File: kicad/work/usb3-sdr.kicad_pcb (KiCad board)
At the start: 4 copper layers, 100 x 60 mm, 231 parts, among them J1 USB3 Micro-B, J2 SMA RF IN, J3 TC2050 JTAG, J4 SMA 10MHz REF, J5 PMOD0, J6 PMOD1, K1 HFD4/5-SR, K2 HFD4/5-SR, Q1 2N7002, Q10 AO3401A, Q11 2N7002, Q2 2N7002, T1 ADT4-6T+, U1 TPS22918DBVR, U10 W25Q128JVSIQ, U11 FT601Q-B-T, U12 LFE5U-25F-6BG256C, U13 PHA-13LN+, U14 74LVC1G17, U2 TPS62A02ADRLR, U3 TPS62A02ADRLR (forced PWM), U4 TLV75525PDBVR, U5 TPS7A2018PDBVR, U6 TPS7A2033PDBVR, U7 TPS7A2018PDBVR, U8 AD9649BCPZ-80, U9 LMK61E2-100M00SIAR, Y1 30MHz 20pF X322530MSB4SI

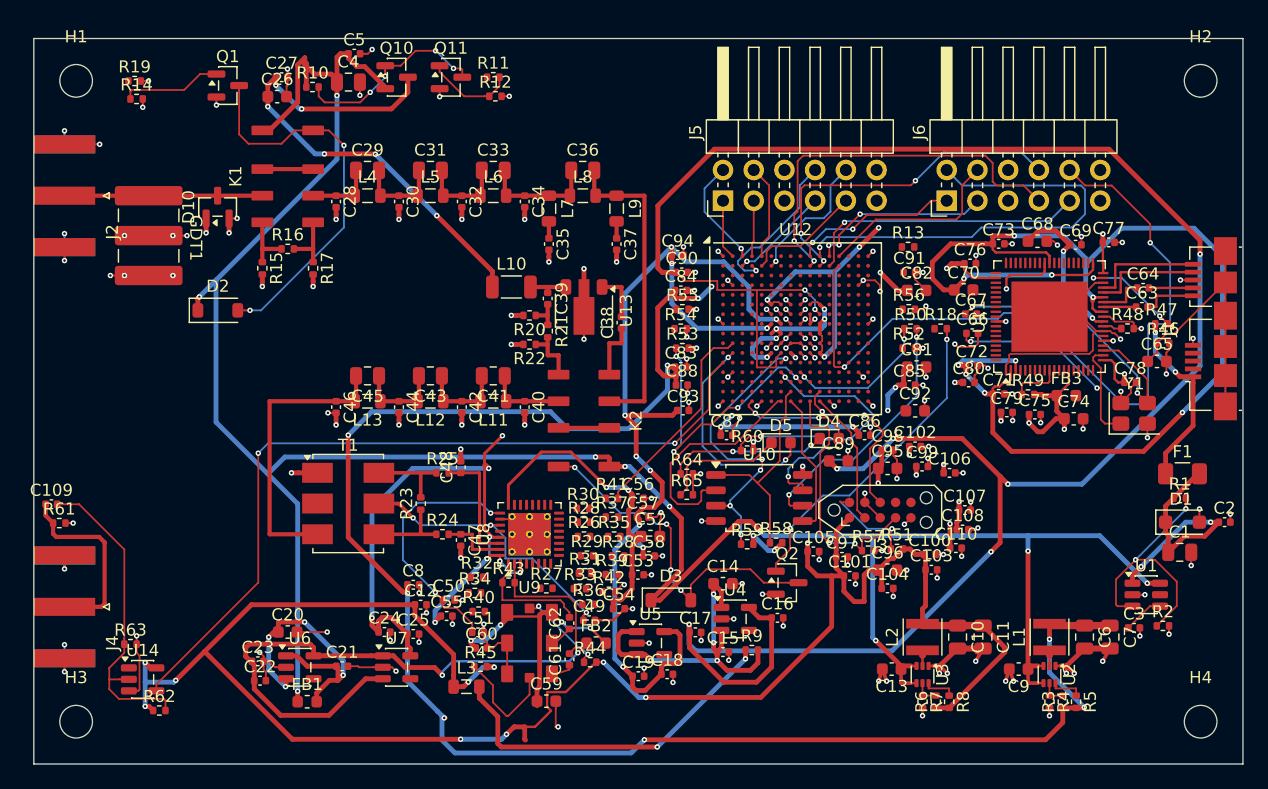
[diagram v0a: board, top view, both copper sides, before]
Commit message: Fan-out v3 applied, DeepPCB runs 3/4 adopted, bus length rules
- AGY fan-out plan v3 (with Claude's fixes) applied: power islands clear of
  the BGA escape rings, all islands fill, 0 copper conflicts.
- DeepPCB run 3 + run 4 adopted into kicad/work: 54 unconnected, DRC clean
  apart from the known SMA edge items; raw inputs/outputs in kicad/deeppcb.
- AGY ADC resistor moves applied; ADC bus re-routed, all routed FT601/ADC
  nets pass the corrected length/skew rules (notes/route).
- New tools: apply_moves.py, edge_keepout.py, lane_clear.py.

Co-Authored-By: Claude Opus 5.5 <noreply@anthropic.com>
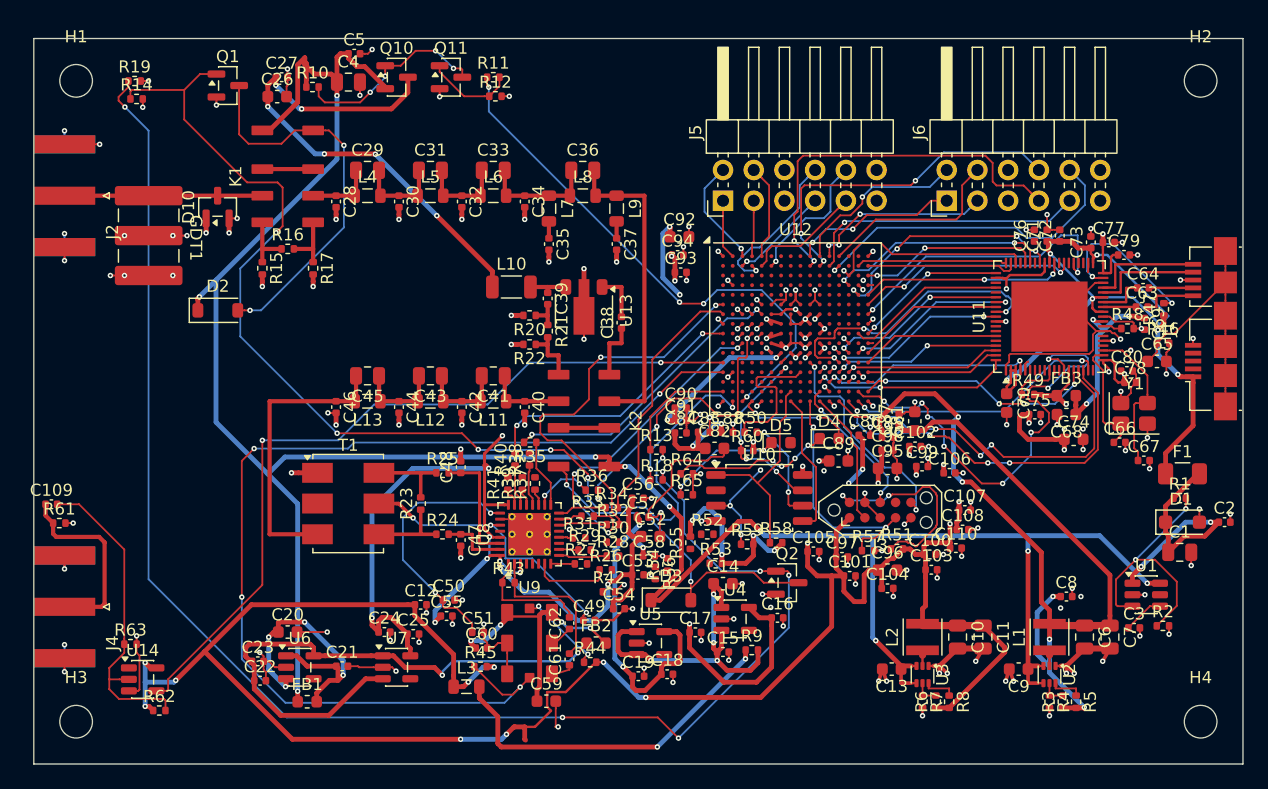
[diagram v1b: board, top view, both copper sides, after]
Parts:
- moved C8 54.0 mm to (185.4, 146.2)
- moved R56 30.2 mm to (151.4, 144.2), turned to -90 degrees
- moved R13 26.7 mm to (151.5, 134.0)
- moved R18 26.6 mm to (151.5, 136.5)
- moved C92 24.2 mm to (153.4, 116.4)
- moved R52 22.7 mm to (155.7, 141.0)
- moved C91 22.5 mm to (153.5, 131.6)
- moved C82 21.2 mm to (156.3, 133.9)
- moved R54 19.5 mm to (152.4, 143.5), turned to 90 degrees
- moved R55 19.3 mm to (154.3, 141.7), turned to 90 degrees
- moved C67 18.7 mm to (191.8, 134.9)
- moved R53 18.0 mm to (156.4, 143.4)
- moved C79 16.2 mm to (190.2, 117.9)
- moved R50 15.7 mm to (159.3, 132.6)
- moved C66 15.2 mm to (189.8, 133.4)
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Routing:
- net 2V5: track 181.4 -> 31.6 mm
- net /RF front end/Q2_G: track 27.2 -> 125.8 mm, vias 2 -> 6
- net LMK_SCL: track 9.20 -> 90.4 mm, vias 0 -> 4
- net /RF front end/Q1_G: track 8.33 -> 85.1 mm, vias 0 -> 6
- net 1V1: track 169.5 -> 99.7 mm, vias 21 -> 16
- net /USB 3 bridge/FT_1V0: track 105.0 -> 46.2 mm, vias 9 -> 4
- net 1V8_D: track 84.5 -> 38.4 mm, vias 10 -> 9
- net LNA_EN: track 0.00 -> 44.7 mm, vias 0 -> 4
- net FT_OE_N: track 0.00 -> 38.4 mm, vias 0 -> 8
- net /FPGA/PMOD1_7: track 64.9 -> 27.6 mm, vias 2 -> 1
- net ADC_D6: track 0.00 -> 32.7 mm, vias 0 -> 2
- net FT_WAKEUP_N: track 0.00 -> 31.1 mm, vias 0 -> 4
- net FT_GPIO0: track 0.00 -> 30.9 mm, vias 0 -> 4
- net ADC_D7: track 0.00 -> 27.5 mm, vias 0 -> 4
- net ADC_D10: track 0.00 -> 25.0 mm, vias 0 -> 3
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- added copper zone on In2.Cu, net 1V8_D
- added copper zone on In2.Cu, net 2V5

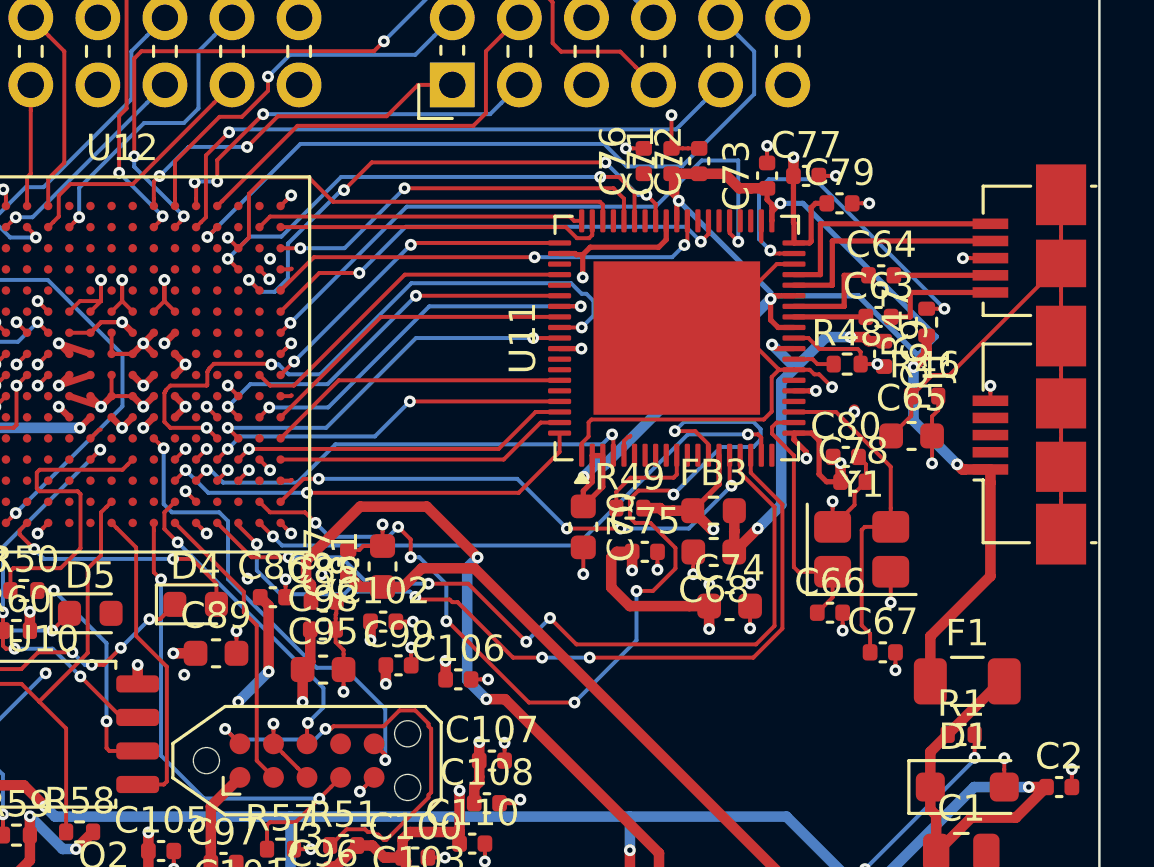
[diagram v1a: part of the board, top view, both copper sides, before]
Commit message: U11 escape plan, USB2 pair route, FT601 centre-pad vias
- AGY U11 (FT601) escape plan applied: all 19 stuck FT601 nets routed,
  every FT bus net passes length/skew (11-28 mm).
- USB2 pair hand-routed (D- crosses under D+ on B.Cu), C65 moved off the
  pair path, VBUS sense branch re-routed.
- U11 centre pad had no vias to the GND plane: 7 GND vias added.
- kicad/gen/u11_trial.py: trial any moves/rips/tracks/vias plan on a temp
  copy with real fill + DRC.
- Work board: 33 unconnected, copper DRC clean, parity 0.

Co-Authored-By: Claude Opus 5.5 <noreply@anthropic.com>
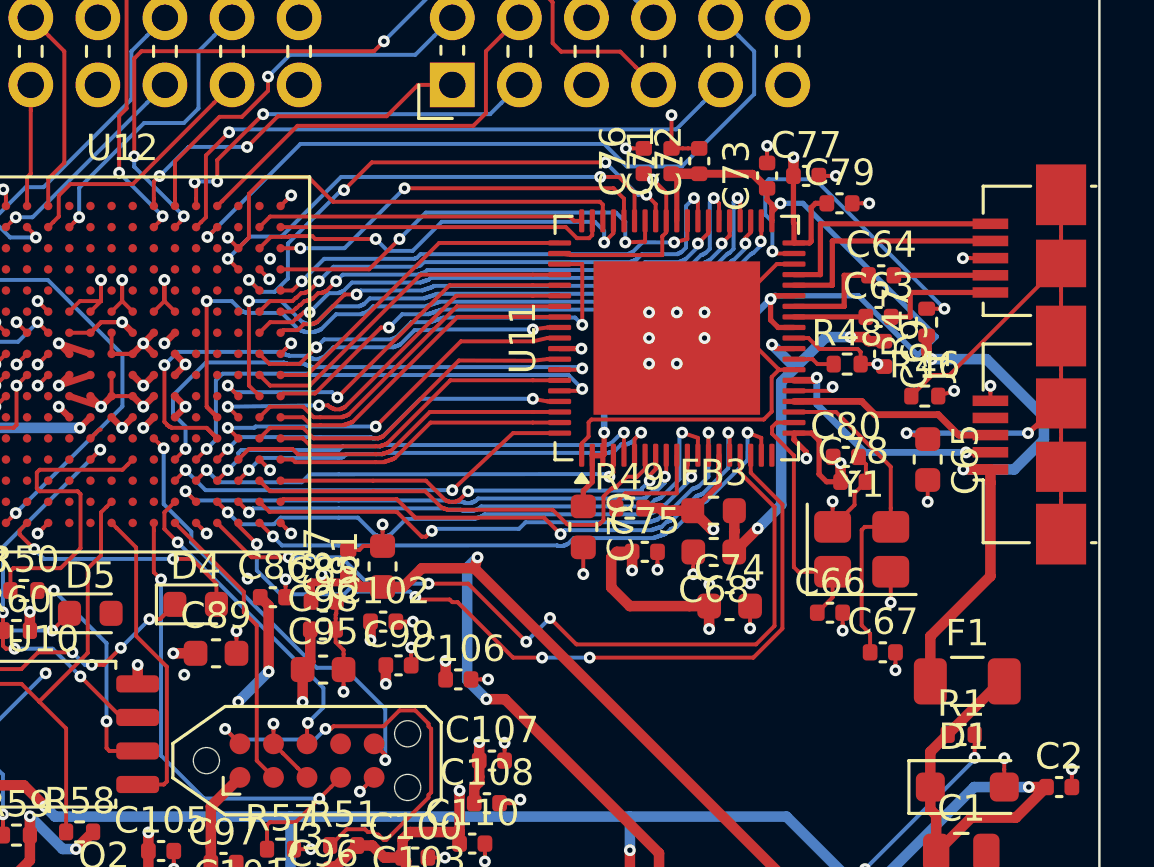
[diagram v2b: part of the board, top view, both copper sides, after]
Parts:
- moved C65 1.08 mm to (193.5, 127.6), turned to -90 degrees
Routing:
- net FT_D1: track 0.57 -> 28.5 mm, vias 1 -> 2
- net FT_D2: track 0.00 -> 26.5 mm, vias 0 -> 2
- net FT_D4: track 0.00 -> 21.3 mm, vias 0 -> 2
- net FT_D0: track 1.24 -> 22.1 mm, vias 0 -> 2
- net FT_RD_N: track 0.00 -> 20.6 mm, vias 0 -> 2
- net FT_WR_N: track 0.00 -> 20.6 mm, vias 0 -> 2
- net FT_D6: track 0.00 -> 20.1 mm, vias 0 -> 2
- net FT_RXF_N: track 0.57 -> 20.3 mm, vias 1 -> 2
- net FT_D25: track 0.57 -> 19.8 mm, vias 1 -> 2
- net FT_D27: track 0.57 -> 18.4 mm, vias 1 -> 2
- net FT_OE_N: track 38.4 -> 21.0 mm, vias 8 -> 2
- net FT_BE3: track 0.00 -> 17.2 mm
- net FT_BE2: track 0.57 -> 17.0 mm, vias 1 -> 2
- net FT_D16: track 0.00 -> 16.4 mm, vias 0 -> 2
- net FT_D9: track 0.44 -> 16.4 mm, vias 0 -> 2
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
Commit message: Route U12 south-west region: board fully routed
AGY's U12 south-west plan round 2 (ADC bus, ADC SPI, FPGA config, flash, LED1,
LMK_SDA, rail stubs) closes the last 33 connections: 0 unconnected, schematic
parity 0, no new copper DRC errors. ADC and FT601 timing pass.

- New kicad/gen/rf_spacing.py: digital copper vs RF-path copper, same layer.
  Round 1 ran ADC lines 0.21 mm beside NOTCH_OUT; round 2 keeps >= 0.65 mm
  and also clears the pre-existing REF10M / LPF2_OUT and ADC_D8 / NOTCH_OUT
  runs. Seven ADC nets run at 0.10 mm width beside NOTCH_OUT.
- In2 rect x 134-152, y 108-134 retargeted from 1V8_A to GND: it had no loads
  and its only feed was ripped by the plan (isolated copper).
- u11_trial.py also prints all still-open nets and ADC timing FAIL lines.
- DeepPCB run 5 input kept (run stopped without a revision).
- Briefs, plans and Claude's reviews in notes/u12sw/; STATUS.md updated.

Co-Authored-By: Claude Opus 5.5 <noreply@anthropic.com>
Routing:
- net ADC_SCLK: track 0.57 -> 39.9 mm, vias 1 -> 2
- net ADC_CSB: track 0.00 -> 39.0 mm, vias 0 -> 2
- net ADC_D0: track 0.57 -> 37.2 mm, vias 1 -> 2
- net ADC_SDIO: track 0.00 -> 36.1 mm, vias 0 -> 2
- net ADC_D12: track 0.57 -> 36.1 mm, vias 1 -> 2
- net LMK_SDA: track 7.10 -> 42.2 mm, vias 2 -> 7
- net ADC_D13: track 0.57 -> 33.7 mm, vias 1 -> 6
- net ADC_D2: track 0.00 -> 32.0 mm, vias 0 -> 2
- net ADC_D11: track 0.57 -> 32.2 mm, vias 1 -> 4
- net ADC_D1: track 0.57 -> 31.1 mm, vias 1 -> 2
- net ADC_D5: track 0.57 -> 30.6 mm, vias 1 -> 2
- net ADC_OR: track 0.00 -> 29.1 mm, vias 0 -> 2
- net /FPGA/FPGA_CFG0: track 0.00 -> 29.0 mm, vias 0 -> 2
- net ADC_D3: track 0.57 -> 29.2 mm, vias 1 -> 2
- net /FPGA/FPGA_DONE: track 0.00 -> 27.1 mm, vias 0 -> 2
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- removed copper zone on In2.Cu, net 1V8_A

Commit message: Remove dangling vias and stubs from the work board
8 vias connected on one layer only (1V1 x2, 2V5 x2, 3V3_D, 5V_SW, FT_D13,
LNA_EN) and 3 stubs left loose by them (3V3_D 0.1 + 1.0 mm, FT_D13 0.57 mm
escape stub). DRC after: 0 unconnected, parity 0, no dangling copper; only
the 10 SMA edge items and silk warnings remain. Timing and RF spacing
unchanged (FT_D13 16.92 mm, pass). Backup kicad/deeppcb/work_before_cleanup.

Co-Authored-By: Claude Opus 5.5 <noreply@anthropic.com>
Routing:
- net 3V3_D: track 228.3 -> 227.2 mm, vias 36 -> 35
- net FT_D13: track 17.5 -> 16.9 mm, vias 1 -> 0
- net LNA_EN: vias 3 -> 2
- net 5V_SW: vias 9 -> 8
- net 2V5: vias 7 -> 5
- net 1V1: vias 14 -> 12
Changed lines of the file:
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@@
 	)
 	(via
-		(at 184.92 147.1)
-		(size 0.45)
-		(drill 0.2)
-		(layers "F.Cu" "B.Cu")
-		(locked yes)
-		(net 121)
-	)
-	(via
 		(at 167.395 136.776)
 		(size 0.45)
@@
 	)
 	(via
-		(at 167.75 132.11)
-		(size 0.45)
-		(drill 0.2)
-		(layers "F.Cu" "B.Cu")
-		(locked yes)
-		(net 121)
-	)
-	(via
 		(at 186.873 155.321)
 		(size 0.45)
@@
 	)
 	(via
-		(at 165.35 135.75)
-		(size 0.45)
-		(drill 0.2)
-		(layers "F.Cu" "B.Cu")
-		(locked yes)
-		(net 124)
-	)
-	(via
 		(at 164.937 134.937)
 		(size 0.45)
@@
 	)
 	(via
-		(at 160.95 147.05)
-		(size 0.45)
-		(drill 0.2)
-		(layers "F.Cu" "B.Cu")
-		(locked yes)
-		(net 124)
-	)
-	(via
 		(at 154.231 148.408)
 		(size 0.45)
@@
 	)
 	(segment
-		(start 140.598 156.93)
-		(end 140.598 157.955)
-		(width 0.4)
-		(layer "F.Cu")
-		(net 126)
-	)
-	(segment
 		(start 171.896 142.214)
 		(end 172.466 142.214)
@@
 	)
 	(segment
-		(start 140.598 157.955)
-		(end 140.668 158.025)
-		(width 0.4)
-		(layer "F.Cu")
-		(net 126)
-	)
-	(segment
 		(start 180 119.86)
 		(end 183.45 119.86)
@@
 	)
 	(via
-		(at 185.23 132.32)
-		(size 0.45)
-		(drill 0.2)
-		(layers "F.Cu" "B.Cu")
-		(locked yes)
-		(net 126)
-	)
-	(via
 		(at 160.6 125.6)
 		(size 0.45)
@@
 	)
 	(via
-		(at 160.076 140.734)
-		(size 0.45)
-		(drill 0.2)
-		(layers "F.Cu" "B.Cu")
-		(net 128)
-	)
-	(via
 		(at 121.822 153.983)
 		(size 0.45)
@@
 	)
 	(segment
-		(start 167.4 119.6)
-		(end 167 119.2)
-		(width 0.15)
-		(locked yes)
-		(layer "F.Cu")
-		(net 169)
-	)
-	(segment
 		(start 181.2 117.949)
 		(end 181.2 118.562)
@@
 		(net 169)
 	)
-	(via
-		(at 167 119.2)
-		(size 0.45)
-		(drill 0.2)
-		(layers "F.Cu" "B.Cu")
-		(locked yes)
-		(net 169)
-	)
 	(segment
 		(start 179.8 118.8)
@@
 		(size 0.45)
 		(drill 0.2)
-		(layers "F.Cu" "B.Cu")
-		(net 200)
-	)
-	(via
-		(at 153.402 121.801)
-		(size 0.45)
-		(drill 0.2)
